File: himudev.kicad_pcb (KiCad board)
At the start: 4 copper layers, 130 parts, among them J1 Conn_01x02, J2 USB_B_Micro, J3 Conn_01x03, J4 20021121-00010C4LF, J5 Conn_02x17_Odd_Even, Q1 IRLML6402, Q2 BSS214NW, Q3 BSS214NW, Q4 BSS214NW, Q5 BSS214NW, Q6 BSS214NW, U1 FT230XS, U2 MCP1726-3302ESN, U3 MIC5319-1.8YD5-TR, U4 IS25WP032D, U5 FE310-G002, U6 ICM-20948, U7 BMP388, X1 KX2132709Z, Y1 TSX-3225 16.0000MF18X-AC0

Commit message: Reload netlist, set part number of J1 and J3
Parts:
- removed C1, C6: 10nF, Capacitor_SMD:C_0805_2012Metric_Pad1.15x1.40mm_HandSolder
- removed C10, C19, C27, C7: 10uF, Capacitor_SMD:C_0805_2012Metric_Pad1.15x1.40mm_HandSolder
- removed C11, C13, C17, C21, C23, C24, C5, C9: 0.1uF, Capacitor_SMD:C_0805_2012Metric_Pad1.15x1.40mm_HandSolder
- removed C12, C15, C20, C22, C25, C26: 1uF, Capacitor_SMD:C_0805_2012Metric_Pad1.15x1.40mm_HandSolder
- removed C14: 2.2uF, Capacitor_SMD:C_0805_2012Metric_Pad1.15x1.40mm_HandSolder
- removed C16, C18: 15pF, Capacitor_SMD:C_0805_2012Metric_Pad1.15x1.40mm_HandSolder
- removed C2, C4: 47pF, Capacitor_SMD:C_0805_2012Metric_Pad1.15x1.40mm_HandSolder
- removed C28, C29, C31, C34: 0.1u, Capacitor_SMD:C_0805_2012Metric_Pad1.15x1.40mm_HandSolder
- removed C3: 4.7uF, Capacitor_SMD:C_0805_2012Metric_Pad1.15x1.40mm_HandSolder
- removed C30, C32, C33: 100n, Capacitor_SMD:C_0805_2012Metric_Pad1.15x1.40mm_HandSolder
- removed C8: 1nF, Capacitor_SMD:C_0805_2012Metric_Pad1.15x1.40mm_HandSolder
- removed D1: NSR05T40XV2T5G, Diode_SMD:D_SOD-523
- removed D10, D9: PESD0603-240, Diode_SMD:D_0603_1608Metric_Pad1.05x0.95mm_HandSolder
- removed D11, D6: Red LTST-C170KRKT, LED_SMD:LED_0805_2012Metric_Pad1.15x1.40mm_HandSolder
- removed D12, D3, D5: Green LTST-C170KGKT, LED_SMD:LED_0805_2012Metric_Pad1.15x1.40mm_HandSolder
- removed D13: Blue LTST-C170TBKT, LED_SMD:LED_0805_2012Metric_Pad1.15x1.40mm_HandSolder
- removed D14, D8: Yellow LTST-C170KSKT, LED_SMD:LED_0805_2012Metric_Pad1.15x1.40mm_HandSolder
- removed D2: SP0502BAHT, Package_TO_SOT_SMD:SOT-23
- removed D4, D7: Orange LTST-C170KFKT, LED_SMD:LED_0805_2012Metric_Pad1.15x1.40mm_HandSolder
- removed FB1: MI0805K601R-10, Resistor_SMD:R_0805_2012Metric_Pad1.15x1.40mm_HandSolder
- removed J1: Conn_01x02, Connector_PinHeader_2.54mm:PinHeader_1x02_P2.54mm_Vertical_SMD_Pin1Left
- removed J2: USB_B_Micro, Connector_USB:USB_Micro-B_Molex-105017-0001
- removed J3: Conn_01x03, Connector_PinHeader_2.54mm:PinHeader_1x03_P2.54mm_Vertical_SMD_Pin1Left
- removed J4: 20021121-00010C4LF, digikey-footprints:PinHeader_2x5_P1.27mm
- removed J5: Conn_02x17_Odd_Even, Connector_PinHeader_2.54mm:PinHeader_2x17_P2.54mm_Vertical_SMD
- removed Q1: IRLML6402, Package_TO_SOT_SMD:SOT-23
- removed Q2, Q3, Q4, Q5, Q6: BSS214NW, Package_TO_SOT_SMD:SOT-323_SC-70
- removed R1, R10, R11, R2, R3, R4, R47, R5, R50, R6, R7, R8, R9: 0, Resistor_SMD:R_0805_2012Metric_Pad1.15x1.40mm_HandSolder
- removed R12, R13: 27, Resistor_SMD:R_0805_2012Metric_Pad1.15x1.40mm_HandSolder
- removed R14, R15, R22: 10k, Resistor_SMD:R_0805_2012Metric_Pad1.15x1.40mm_HandSolder
- removed R16, R20, R27, R29, R30, R31: 100k, Resistor_SMD:R_0805_2012Metric_Pad1.15x1.40mm_HandSolder
- removed R17: 1k, Resistor_SMD:R_0805_2012Metric_Pad1.15x1.40mm_HandSolder
- removed R18, R19, R23, R26, R40, R42, R44, R46: 270, Resistor_SMD:R_0805_2012Metric_Pad1.15x1.40mm_HandSolder
- removed R21, R32, R33, R34, R35, R36, R37, R38, R39, R41, R43, R45: 100, Resistor_SMD:R_0805_2012Metric_Pad1.15x1.40mm_HandSolder
- removed R24, R25: 560, Resistor_SMD:R_0805_2012Metric_Pad1.15x1.40mm_HandSolder
- removed R28: 1M, Resistor_SMD:R_0805_2012Metric_Pad1.15x1.40mm_HandSolder
- removed R48, R49: 4k7, Resistor_SMD:R_0805_2012Metric_Pad1.15x1.40mm_HandSolder
- removed S1, S2: B3F-1000, digikey-footprints:Switch_Tactile_THT_B3F-1xxx
- removed TP1: GND, TestPoint:TestPoint_Pad_D1.5mm
- removed TP2: VBUS, TestPoint:TestPoint_Pad_D1.5mm
- removed TP3: 3V3, TestPoint:TestPoint_Pad_D1.5mm
- removed TP4: FTDI_CBUS0, TestPoint:TestPoint_Pad_D1.5mm
- removed TP5: FTDI_RTS#, TestPoint:TestPoint_Pad_D1.5mm
- removed TP6: FTDI_CTS#, TestPoint:TestPoint_Pad_D1.5mm
- removed TP7: 5V, TestPoint:TestPoint_Pad_D1.5mm
- removed TP8: 1V8, TestPoint:TestPoint_Pad_D1.5mm
- removed TP9: LFALTCLK, TestPoint:TestPoint_Pad_D1.5mm
- removed U1: FT230XS, Package_SO:SSOP-16_3.9x4.9mm_P0.635mm
- removed U2: MCP1726-3302ESN, Package_SO:SOIC-8_3.9x4.9mm_P1.27mm
- removed U3: MIC5319-1.8YD5-TR, Package_TO_SOT_SMD:TSOT-23-5
- removed U4: IS25WP032D, Package_SO:SOIC-8_3.9x4.9mm_P1.27mm
- removed U5: FE310-G002, himudev:QFN-48-1EP_6x6mm_P0.4mm_EP4.2x4.2mm_BigVia
- removed U6: ICM-20948, Sensor_Motion:InvenSense_QFN-24_3x3mm_P0.4mm
- removed U7: BMP388, himudev:Bosch_LGA-10_2x2mm_P0.5mm
- removed X1: KX2132709Z, himudev:KX2132709Z
- removed Y1: TSX-3225 16.0000MF18X-AC0, himudev:TSX-3225

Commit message: Placed component footprints in logical groups
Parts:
- added C1: 10nF, Capacitor_SMD:C_0805_2012Metric_Pad1.15x1.40mm_HandSolder, F.Cu at (76.5, 97.3)
- added C10: 10uF, Capacitor_SMD:C_0805_2012Metric_Pad1.15x1.40mm_HandSolder, F.Cu at (103.9, 69.6)
- added C11: 0.1uF, Capacitor_SMD:C_0805_2012Metric_Pad1.15x1.40mm_HandSolder, F.Cu at (99.7, 105.7)
- added C12: 1uF, Capacitor_SMD:C_0805_2012Metric_Pad1.15x1.40mm_HandSolder, F.Cu at (130.8, -45.0)
- added C13: 0.1uF, Capacitor_SMD:C_0805_2012Metric_Pad1.15x1.40mm_HandSolder, F.Cu at (140.0, -38.9)
- added C14: 2.2uF, Capacitor_SMD:C_0805_2012Metric_Pad1.15x1.40mm_HandSolder, F.Cu at (147.1, -46.7)
- added C15: 1uF, Capacitor_SMD:C_0805_2012Metric_Pad1.15x1.40mm_HandSolder, F.Cu at (163.8, 112.3)
- added C16: 15pF, Capacitor_SMD:C_0805_2012Metric_Pad1.15x1.40mm_HandSolder, F.Cu at (153.2, 131.6)
- added C17: 0.1uF, Capacitor_SMD:C_0805_2012Metric_Pad1.15x1.40mm_HandSolder, F.Cu at (190.2, 146.8)
- added C18: 15pF, Capacitor_SMD:C_0805_2012Metric_Pad1.15x1.40mm_HandSolder, F.Cu at (157.9, 131.6)
- added C19: 10uF, Capacitor_SMD:C_0805_2012Metric_Pad1.15x1.40mm_HandSolder, F.Cu at (164.6, 44.2)
- added C2: 47pF, Capacitor_SMD:C_0805_2012Metric_Pad1.15x1.40mm_HandSolder, F.Cu at (80.5, 107.7)
- added C20: 1uF, Capacitor_SMD:C_0805_2012Metric_Pad1.15x1.40mm_HandSolder, F.Cu at (164.6, 47.8)
- added C21: 0.1uF, Capacitor_SMD:C_0805_2012Metric_Pad1.15x1.40mm_HandSolder, F.Cu at (164.6, 51.4)
- added C22: 1uF, Capacitor_SMD:C_0805_2012Metric_Pad1.15x1.40mm_HandSolder, F.Cu at (169.7, 51.6)
- added C23: 0.1uF, Capacitor_SMD:C_0805_2012Metric_Pad1.15x1.40mm_HandSolder, F.Cu at (175.5, 51.6)
- added C24: 0.1uF, Capacitor_SMD:C_0805_2012Metric_Pad1.15x1.40mm_HandSolder, F.Cu at (180.1, 51.6)
- added C25: 1uF, Capacitor_SMD:C_0805_2012Metric_Pad1.15x1.40mm_HandSolder, F.Cu at (175.5, 47.5)
- added C26: 1uF, Capacitor_SMD:C_0805_2012Metric_Pad1.15x1.40mm_HandSolder, F.Cu at (180.1, 48.0)
- added C27: 10uF, Capacitor_SMD:C_0805_2012Metric_Pad1.15x1.40mm_HandSolder, F.Cu at (175.8, 43.9)
- added C28: 0.1u, Capacitor_SMD:C_0805_2012Metric_Pad1.15x1.40mm_HandSolder, F.Cu at (200.2, -73.8)
- added C29: 0.1u, Capacitor_SMD:C_0805_2012Metric_Pad1.15x1.40mm_HandSolder, F.Cu at (195.4, -68.6)
- added C3: 4.7uF, Capacitor_SMD:C_0805_2012Metric_Pad1.15x1.40mm_HandSolder, F.Cu at (99.6, 111.2)
- added C30: 100n, Capacitor_SMD:C_0805_2012Metric_Pad1.15x1.40mm_HandSolder, F.Cu at (200.6, -76.7)
- added C31: 0.1u, Capacitor_SMD:C_0805_2012Metric_Pad1.15x1.40mm_HandSolder, F.Cu at (195.4, -71.6)
- added C32: 100n, Capacitor_SMD:C_0805_2012Metric_Pad1.15x1.40mm_HandSolder, F.Cu at (222.8, -60.2)
- added C33: 100n, Capacitor_SMD:C_0805_2012Metric_Pad1.15x1.40mm_HandSolder, F.Cu at (229.9, -67.8)
- added C34: 0.1u, Capacitor_SMD:C_0805_2012Metric_Pad1.15x1.40mm_HandSolder, F.Cu at (230.1, -64.3)
- added C4: 47pF, Capacitor_SMD:C_0805_2012Metric_Pad1.15x1.40mm_HandSolder, F.Cu at (80.5, 100.8)
- added C5: 0.1uF, Capacitor_SMD:C_0805_2012Metric_Pad1.15x1.40mm_HandSolder, F.Cu at (94.9, 114.0)
- added C6: 10nF, Capacitor_SMD:C_0805_2012Metric_Pad1.15x1.40mm_HandSolder, F.Cu at (108.5, 107.5)
- added C7: 10uF, Capacitor_SMD:C_0805_2012Metric_Pad1.15x1.40mm_HandSolder, F.Cu at (100.3, 62.5)
- added C8: 1nF, Capacitor_SMD:C_0805_2012Metric_Pad1.15x1.40mm_HandSolder, F.Cu at (103.1, 65.8)
- added C9: 0.1uF, Capacitor_SMD:C_0805_2012Metric_Pad1.15x1.40mm_HandSolder, F.Cu at (95.6, 96.5)
- added D1: NSR05T40XV2T5G, Diode_SMD:D_SOD-523, F.Cu at (75.7, 129.8)
- added D10: PESD0603-240, Diode_SMD:D_0603_1608Metric_Pad1.05x0.95mm_HandSolder, F.Cu at (222.5, 163.8)
- added D11: Red LTST-C170KRKT, LED_SMD:LED_0805_2012Metric_Pad1.15x1.40mm_HandSolder, F.Cu at (174.0, 75.9)
- added D12: Green LTST-C170KGKT, LED_SMD:LED_0805_2012Metric_Pad1.15x1.40mm_HandSolder, F.Cu at (178.1, 75.7)
- added D13: Blue LTST-C170TBKT, LED_SMD:LED_0805_2012Metric_Pad1.15x1.40mm_HandSolder, F.Cu at (182.4, 75.7)
- added D14: Yellow LTST-C170KSKT, LED_SMD:LED_0805_2012Metric_Pad1.15x1.40mm_HandSolder, F.Cu at (186.7, 76.2)
- added D2: SP0502BAHT, Package_TO_SOT_SMD:SOT-23, F.Cu at (79.5, 129.0)
- added D3: Green LTST-C170KGKT, LED_SMD:LED_0805_2012Metric_Pad1.15x1.40mm_HandSolder, F.Cu at (109.7, 98.5)
- added D4: Orange LTST-C170KFKT, LED_SMD:LED_0805_2012Metric_Pad1.15x1.40mm_HandSolder, F.Cu at (104.3, 103.0)
- added D5: Green LTST-C170KGKT, LED_SMD:LED_0805_2012Metric_Pad1.15x1.40mm_HandSolder, F.Cu at (91.2, -13.0)
- added D6: Red LTST-C170KRKT, LED_SMD:LED_0805_2012Metric_Pad1.15x1.40mm_HandSolder, F.Cu at (90.9, -8.89)
- added D7: Orange LTST-C170KFKT, LED_SMD:LED_0805_2012Metric_Pad1.15x1.40mm_HandSolder, F.Cu at (91.2, -5.08)
- added D8: Yellow LTST-C170KSKT, LED_SMD:LED_0805_2012Metric_Pad1.15x1.40mm_HandSolder, F.Cu at (90.9, -1.02)
- added D9: PESD0603-240, Diode_SMD:D_0603_1608Metric_Pad1.05x0.95mm_HandSolder, F.Cu at (172.7, 163.6)
- added FB1: MI0805K601R-10, Resistor_SMD:R_0805_2012Metric_Pad1.15x1.40mm_HandSolder, F.Cu at (88.9, 88.6)
- added J1: M20-8770642R, Connector_PinHeader_2.54mm:PinHeader_1x02_P2.54mm_Vertical_SMD_Pin1Left, F.Cu at (72.9, 124.0)
- added J2: USB_B_Micro, Connector_USB:USB_Micro-B_Molex-105017-0001, F.Cu at (72.6, 105.0)
- added J3: M20-8770642R, Connector_PinHeader_2.54mm:PinHeader_1x03_P2.54mm_Vertical_SMD_Pin1Left, F.Cu at (80.0, 89.4)
- added J4: 20021121-00010C4LF, digikey-footprints:PinHeader_2x5_P1.27mm, F.Cu at (151.6, 162.1)
- added J5: M20-8762042, Connector_PinHeader_2.54mm:PinHeader_2x17_P2.54mm_Vertical_SMD, F.Cu at (210.1, 104.6)
- added Q1: IRLML6402, Package_TO_SOT_SMD:SOT-23, F.Cu at (104.9, 112.6)
- added Q2: BSS214NW, Package_TO_SOT_SMD:SOT-323_SC-70, F.Cu at (86.6, -13.0)
- added Q3: BSS214NW, Package_TO_SOT_SMD:SOT-323_SC-70, F.Cu at (174.0, 80.3)
- added Q4: BSS214NW, Package_TO_SOT_SMD:SOT-323_SC-70, F.Cu at (178.1, 80.0)
- added Q5: BSS214NW, Package_TO_SOT_SMD:SOT-323_SC-70, F.Cu at (182.4, 80.5)
- added Q6: BSS214NW, Package_TO_SOT_SMD:SOT-323_SC-70, F.Cu at (186.7, 80.5)
- added R1: 0, Resistor_SMD:R_0805_2012Metric_Pad1.15x1.40mm_HandSolder, F.Cu at (165.2, -24.0)
- added R10: 0, Resistor_SMD:R_0805_2012Metric_Pad1.15x1.40mm_HandSolder, F.Cu at (160.5, -21.0)
- added R11: 0, Resistor_SMD:R_0805_2012Metric_Pad1.15x1.40mm_HandSolder, F.Cu at (160.5, -24.0)
- added R12: 27, Resistor_SMD:R_0805_2012Metric_Pad1.15x1.40mm_HandSolder, F.Cu at (80.5, 105.4)
- added R13: 27, Resistor_SMD:R_0805_2012Metric_Pad1.15x1.40mm_HandSolder, F.Cu at (80.5, 103.1)
- added R14: 10k, Resistor_SMD:R_0805_2012Metric_Pad1.15x1.40mm_HandSolder, F.Cu at (104.6, 107.4)
- added R15: 10k, Resistor_SMD:R_0805_2012Metric_Pad1.15x1.40mm_HandSolder, F.Cu at (96.0, 63.0)
- added R16: 100k, Resistor_SMD:R_0805_2012Metric_Pad1.15x1.40mm_HandSolder, F.Cu at (100.1, 100.9)
- added R17: 1k, Resistor_SMD:R_0805_2012Metric_Pad1.15x1.40mm_HandSolder, F.Cu at (100.3, 96.8)
- added R18: 270, Resistor_SMD:R_0805_2012Metric_Pad1.15x1.40mm_HandSolder, F.Cu at (90.1, 117.1)
- added R19: 270, Resistor_SMD:R_0805_2012Metric_Pad1.15x1.40mm_HandSolder, F.Cu at (94.9, 111.1)
- added R2: 0, Resistor_SMD:R_0805_2012Metric_Pad1.15x1.40mm_HandSolder, F.Cu at (160.5, -18.1)
- added R20: 100k, Resistor_SMD:R_0805_2012Metric_Pad1.15x1.40mm_HandSolder, F.Cu at (95.5, 116.9)
- added R21: 100, Resistor_SMD:R_0805_2012Metric_Pad1.15x1.40mm_HandSolder, F.Cu at (82.5, -13.0)
- added R22: 10k, Resistor_SMD:R_0805_2012Metric_Pad1.15x1.40mm_HandSolder, F.Cu at (145.8, -41.9)
- added R23: 270, Resistor_SMD:R_0805_2012Metric_Pad1.15x1.40mm_HandSolder, F.Cu at (96.0, -13.0)
- added R24: 560, Resistor_SMD:R_0805_2012Metric_Pad1.15x1.40mm_HandSolder, F.Cu at (96.0, -8.89)
- added R25: 560, Resistor_SMD:R_0805_2012Metric_Pad1.15x1.40mm_HandSolder, F.Cu at (96.0, -5.08)
- added R26: 270, Resistor_SMD:R_0805_2012Metric_Pad1.15x1.40mm_HandSolder, F.Cu at (96.0, -1.02)
- added R27: 100k, Resistor_SMD:R_0805_2012Metric_Pad1.15x1.40mm_HandSolder, F.Cu at (173.5, 160.3)
- added R28: 1M, Resistor_SMD:R_0805_2012Metric_Pad1.15x1.40mm_HandSolder, F.Cu at (155.2, 135.4)
- added R29: 100k, Resistor_SMD:R_0805_2012Metric_Pad1.15x1.40mm_HandSolder, F.Cu at (162.1, 102.1)
- added R3: 0, Resistor_SMD:R_0805_2012Metric_Pad1.15x1.40mm_HandSolder, F.Cu at (165.2, -21.0)
- added R30: 100k, Resistor_SMD:R_0805_2012Metric_Pad1.15x1.40mm_HandSolder, F.Cu at (166.4, 102.9)
- added R31: 100k, Resistor_SMD:R_0805_2012Metric_Pad1.15x1.40mm_HandSolder, F.Cu at (223.5, 159.8)
- added R32: 100, Resistor_SMD:R_0805_2012Metric_Pad1.15x1.40mm_HandSolder, F.Cu at (144.5, 159.2)
- added R33: 100, Resistor_SMD:R_0805_2012Metric_Pad1.15x1.40mm_HandSolder, F.Cu at (149.3, 156.2)
- added R34: 100, Resistor_SMD:R_0805_2012Metric_Pad1.15x1.40mm_HandSolder, F.Cu at (144.5, 156.2)
- added R35: 100, Resistor_SMD:R_0805_2012Metric_Pad1.15x1.40mm_HandSolder, F.Cu at (149.3, 153.3)
- added R36: 100, Resistor_SMD:R_0805_2012Metric_Pad1.15x1.40mm_HandSolder, F.Cu at (180.3, 43.9)
- added R37: 100, Resistor_SMD:R_0805_2012Metric_Pad1.15x1.40mm_HandSolder, F.Cu at (198.1, 107.2)
- added R38: 100, Resistor_SMD:R_0805_2012Metric_Pad1.15x1.40mm_HandSolder, F.Cu at (198.2, 111.0)
- added R39: 100, Resistor_SMD:R_0805_2012Metric_Pad1.15x1.40mm_HandSolder, F.Cu at (173.2, 85.3)
- added R4: 0, Resistor_SMD:R_0805_2012Metric_Pad1.15x1.40mm_HandSolder, F.Cu at (170.0, -24.0)
- added R40: 270, Resistor_SMD:R_0805_2012Metric_Pad1.15x1.40mm_HandSolder, F.Cu at (174.0, 71.9)
- added R41: 100, Resistor_SMD:R_0805_2012Metric_Pad1.15x1.40mm_HandSolder, F.Cu at (177.3, 85.3)
- added R42: 270, Resistor_SMD:R_0805_2012Metric_Pad1.15x1.40mm_HandSolder, F.Cu at (178.1, 71.6)
- added R43: 100, Resistor_SMD:R_0805_2012Metric_Pad1.15x1.40mm_HandSolder, F.Cu at (181.6, 85.6)
- added R44: 270, Resistor_SMD:R_0805_2012Metric_Pad1.15x1.40mm_HandSolder, F.Cu at (182.4, 71.4)
- added R45: 100, Resistor_SMD:R_0805_2012Metric_Pad1.15x1.40mm_HandSolder, F.Cu at (185.9, 85.6)
- added R46: 270, Resistor_SMD:R_0805_2012Metric_Pad1.15x1.40mm_HandSolder, F.Cu at (186.7, 71.4)
- added R47: 0, Resistor_SMD:R_0805_2012Metric_Pad1.15x1.40mm_HandSolder, F.Cu at (191.0, -81.0)
- added R48: 4k7, Resistor_SMD:R_0805_2012Metric_Pad1.15x1.40mm_HandSolder, F.Cu at (216.7, -66.3)
- added R49: 4k7, Resistor_SMD:R_0805_2012Metric_Pad1.15x1.40mm_HandSolder, F.Cu at (216.9, -62.5)
- added R5: 0, Resistor_SMD:R_0805_2012Metric_Pad1.15x1.40mm_HandSolder, F.Cu at (165.2, -18.1)
- added R50: 0, Resistor_SMD:R_0805_2012Metric_Pad1.15x1.40mm_HandSolder, F.Cu at (222.8, -69.3)
- added R6: 0, Resistor_SMD:R_0805_2012Metric_Pad1.15x1.40mm_HandSolder, F.Cu at (170.0, -21.0)
- added R7: 0, Resistor_SMD:R_0805_2012Metric_Pad1.15x1.40mm_HandSolder, F.Cu at (174.7, -24.0)
- added R8: 0, Resistor_SMD:R_0805_2012Metric_Pad1.15x1.40mm_HandSolder, F.Cu at (170.0, -18.1)
- added R9: 0, Resistor_SMD:R_0805_2012Metric_Pad1.15x1.40mm_HandSolder, F.Cu at (174.7, -21.0)
- added S1: PTS645SM43SMTR92_LFS, digikey-footprints:Switch_Tactile_SMD_6x6mm_PTS645, F.Cu at (180.0, 162.0)
- added S2: PTS645SM43SMTR92_LFS, digikey-footprints:Switch_Tactile_SMD_6x6mm_PTS645, F.Cu at (215.6, 162.0)
- added TP1: GND, TestPoint:TestPoint_Pad_D1.5mm, F.Cu at (71.9, 98.3)
- added TP2: VBUS, TestPoint:TestPoint_Pad_D1.5mm, F.Cu at (81.8, 82.5)
- added TP3: 3V3, TestPoint:TestPoint_Pad_D1.5mm, F.Cu at (105.2, 62.7)
- added TP4: FTDI_CBUS0, TestPoint:TestPoint_Pad_D1.5mm, F.Cu at (123.4, 105.6)
- added TP5: FTDI_RTS#, TestPoint:TestPoint_Pad_D1.5mm, F.Cu at (117.8, 111.0)
- added TP6: FTDI_CTS#, TestPoint:TestPoint_Pad_D1.5mm, F.Cu at (100.4, 116.4)
- added TP7: 5V, TestPoint:TestPoint_Pad_D1.5mm, F.Cu at (117.1, 115.1)
- added TP8: 1V8, TestPoint:TestPoint_Pad_D1.5mm, F.Cu at (151.9, -42.9)
- added TP9: LFALTCLK, TestPoint:TestPoint_Pad_D1.5mm, F.Cu at (194.1, 142.5)
- added U1: FT230XS, Package_SO:SSOP-16_3.9x4.9mm_P0.635mm, F.Cu at (93.7, 104.9)
- added U2: MCP1726-3302ESN, Package_SO:SOIC-8_3.9x4.9mm_P1.27mm, F.Cu at (96.9, 69.2)
- added U3: MIC5319-1.8YD5-TR, Package_TO_SOT_SMD:TSOT-23-5, F.Cu at (139.4, -45.5)
- added U4: IS25WP032D, Package_SO:SOIC-8_3.9x4.9mm_P1.27mm, F.Cu at (164.3, 107.4)
- added U5: FE310-G002, himudev:QFN-48-1EP_6x6mm_P0.4mm_EP4.2x4.2mm_BigVia, F.Cu at (182.4, 119.4)
- added U6: ICM-20948, Sensor_Motion:InvenSense_QFN-24_3x3mm_P0.4mm, F.Cu at (190.9, -75.6)
- added U7: BMP388, himudev:Bosch_LGA-10_2x2mm_P0.5mm, F.Cu at (223.0, -64.8)
- added X1: KX2132709Z, himudev:KX2132709Z, F.Cu at (190.2, 143.5)
- added Y1: TSX-3225 16.0000MF18X-AC0, himudev:TSX-3225, F.Cu at (164.6, 129.3)
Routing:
- net Net-(TP9-Pad1): track 0.00 -> 2.57 mm
- net GND: track 0.00 -> 2.40 mm
- net +3V3: track 0.00 -> 2.40 mm
- net Net-(C32-Pad2): track 0.00 -> 1.73 mm
- net (no net): vias 0 -> 3

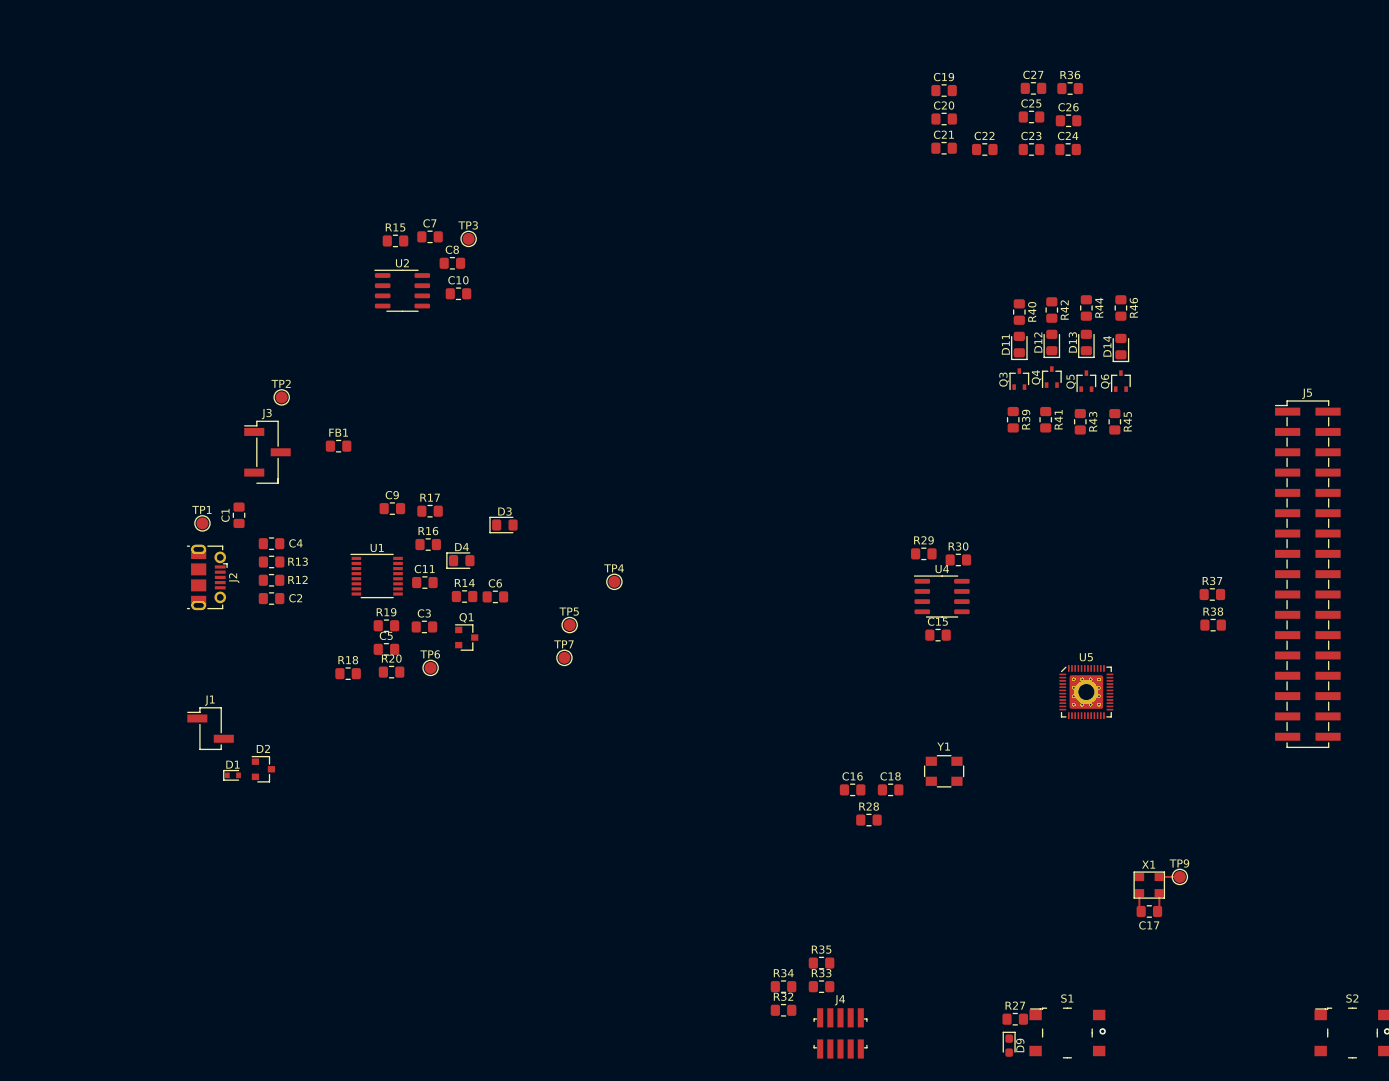
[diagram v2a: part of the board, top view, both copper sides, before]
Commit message: Changed main header from 34 to 32 pin, added board outline
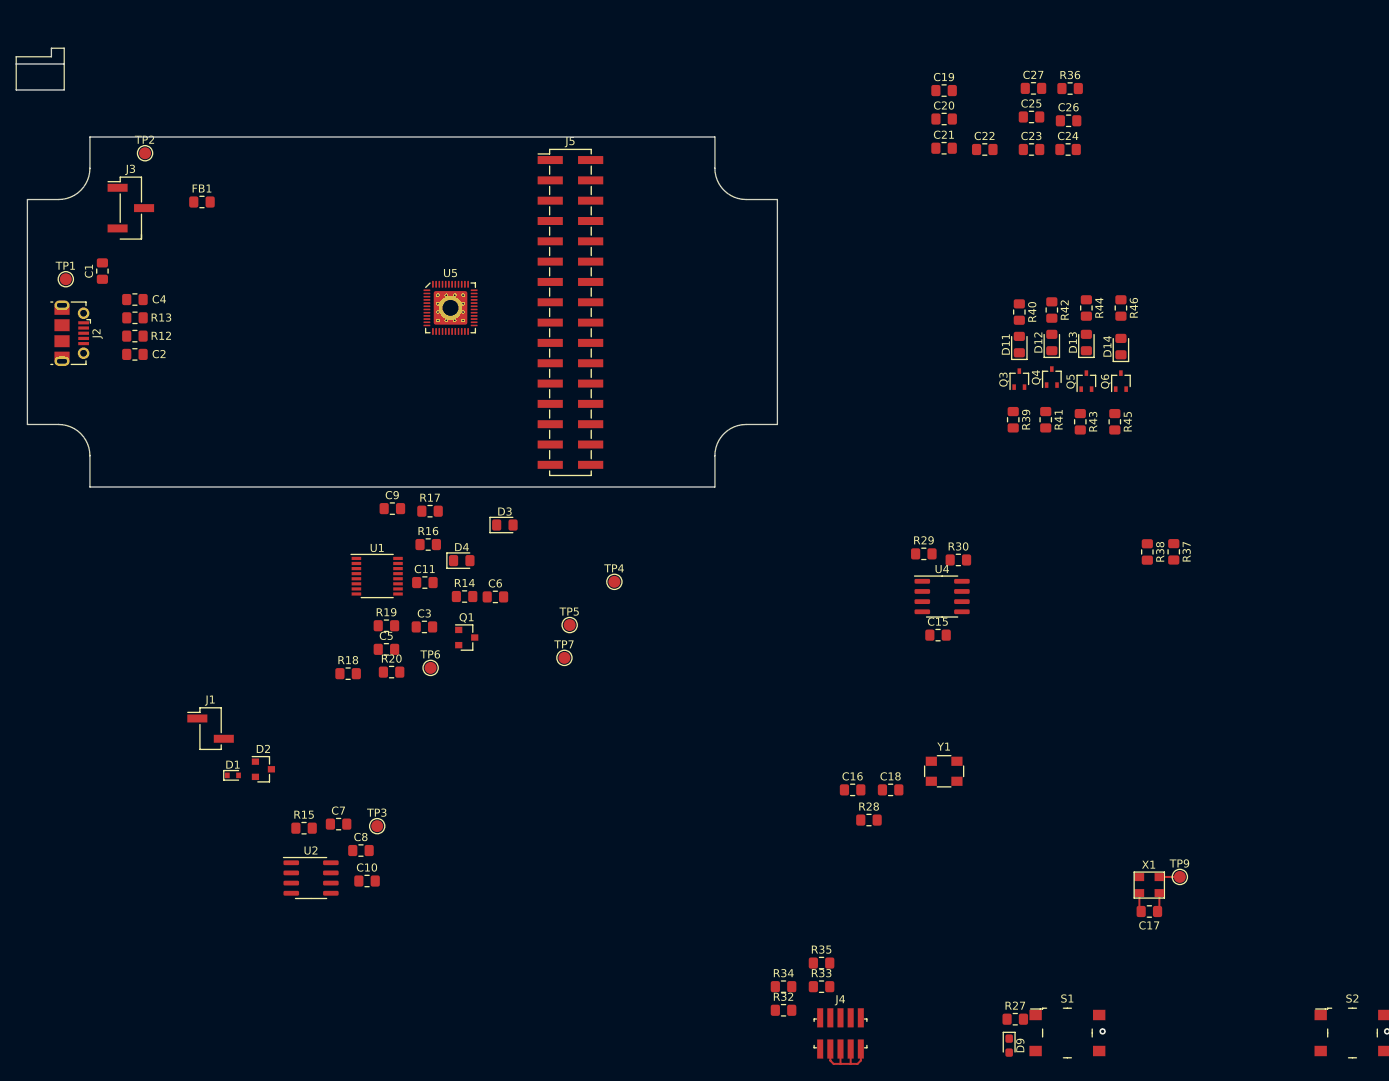
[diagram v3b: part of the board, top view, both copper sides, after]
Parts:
- J5: footprint Connector_PinHeader_2.54mm:PinHeader_2x17_P2.54mm_Vertical_SMD -> Connector_PinHeader_2.54mm:PinHeader_2x16_P2.54mm_Vertical_SMD
- moved J5 97.8 mm to (117.9, 71.9)
- moved U5 92.9 mm to (102.9, 71.4)
- moved R15 74.3 mm to (84.6, 136.4)
- moved TP3 74.3 mm to (93.7, 136.1)
- moved C10 74.3 mm to (92.5, 143.0)
- moved C8 74.3 mm to (91.7, 139.2)
- moved U2 74.3 mm to (85.5, 142.6)
- moved C7 74.3 mm to (88.9, 135.9)
- moved FB1 35.0 mm to (71.8, 58.1)
- moved J2 35.0 mm to (55.6, 74.5)
- moved J3 35.0 mm to (62.9, 58.9)
- moved C2 35.0 mm to (63.4, 77.2)
- moved C4 35.0 mm to (63.4, 70.3)
- moved R12 35.0 mm to (63.4, 74.9)
- moved R13 35.0 mm to (63.4, 72.6)
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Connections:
- J5 pad 13: Net-(J5-Pad13) -> GND
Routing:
- net GND: track 2.40 -> 13.2 mm
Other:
- board outline added: 95.2 x 54.9 mm

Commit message: Placed pressure sensor, connector changed to USB-C
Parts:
- added R51: 5k1, Resistor_SMD:R_0805_2012Metric_Pad1.15x1.40mm_HandSolder, F.Cu at (116.6, 107.3)
- added R52: 5k1, Resistor_SMD:R_0805_2012Metric_Pad1.15x1.40mm_HandSolder, F.Cu at (116.6, 95.9)
- J2: value USB_B_Micro -> USB_C16PIN; footprint Connector_USB:USB_Micro-B_Molex-105017-0001 -> USB-C-16pin:USB-C-COM-15111
- moved C20 236.5 mm to (167.8, -188.7)
- moved R29 236.5 mm to (165.2, -134.4)
- moved R30 236.5 mm to (169.5, -133.6)
- moved R36 236.5 mm to (183.5, -192.5)
- moved R38 236.5 mm to (193.2, -134.6)
- moved R40 236.5 mm to (177.2, -164.6)
- moved C15 236.5 mm to (167.0, -124.2)
- moved C19 236.5 mm to (167.8, -192.3)
- moved C21 236.5 mm to (167.8, -185.1)
- moved C22 236.5 mm to (172.8, -184.9)
- moved C23 236.5 mm to (178.7, -184.9)
- moved C24 236.5 mm to (183.3, -184.9)
- moved C25 236.5 mm to (178.7, -189.0)
- moved C26 236.5 mm to (183.3, -188.5)
- moved C27 236.5 mm to (178.9, -192.6)
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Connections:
- C2 pad 1: Net-(C2-Pad1) -> /USB_Power/USB_D+
- C4 pad 1: Net-(C4-Pad1) -> /USB_Power/USB_D-
- R12 pad 2: Net-(C2-Pad1) -> /USB_Power/USB_D+
- R13 pad 2: Net-(C4-Pad1) -> /USB_Power/USB_D-
- R48 pad 1: +3V3 -> Net-(C32-Pad2)
- R49 pad 1: +3V3 -> Net-(C32-Pad2)
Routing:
- net GND: track 13.2 -> 41.6 mm, vias 0 -> 11
- net Net-(C32-Pad2): track 1.73 -> 28.8 mm
- net Net-(C1-Pad1): track 0.00 -> 24.8 mm, vias 0 -> 2
- net /Sensors/BMP_INT: track 0.00 -> 15.2 mm
- net /Sensors/BMP_SCL: track 0.00 -> 12.5 mm, vias 0 -> 2
- net /MCU_clk_reset/I2C_SDA: track 0.00 -> 10.9 mm
- net /Sensors/BMP_SDA: track 0.00 -> 10.5 mm
- net /USB_Power/USB_D-: track 0.00 -> 10.2 mm
- net /USB_Power/USB_D+: track 0.00 -> 8.40 mm
- net Net-(J2-PadA5): track 0.00 -> 7.49 mm
- net VIN: track 0.00 -> 7.36 mm
- net +3V3: track 2.40 -> 9.33 mm
- net Net-(J2-PadB5): track 0.00 -> 6.82 mm
- net /MCU_clk_reset/I2C_INT: track 0.00 -> 6.11 mm
- net /MCU_clk_reset/I2C_SCL: track 0.00 -> 5.26 mm
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- added copper zone on In2.Cu, net +3V3
- added copper zone on In1.Cu, net GND
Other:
- board size 95.2 x 54.9 mm -> 93.6 x 43.6 mm
- net class Default: clearance 0.2 -> 0.254; trace_width 0.25 -> 0.254; via_dia 0.8 -> 0.508; via_drill 0.4 -> 0.254
- rule pad_to_mask_clearance: 0.051 -> 0.0889
- rule solder_mask_min_width: 0.25 -> 0.0889
- rule trace_clearance: 0.2 -> 0.254
- rule trace_min: 0.2 -> 0.127
- rule via_min_drill: 0.3 -> 0.254
- rule via_min_size: 0.4 -> 0.508

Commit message: Route power traces on the inner layer
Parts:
- moved TP3 213.6 mm to (145.8, 86.0)
- moved U2 208.6 mm to (129.5, 87.1), turned to 270 degrees
- moved C10 205.5 mm to (133.7, 88.9), turned to 90 degrees
- moved R15 203.0 mm to (125.6, 87.6), turned to 90 degrees
- moved C7 200.7 mm to (125.6, 83.4), turned to 270 degrees
- moved C8 198.3 mm to (128.3, 91.9), turned to 180 degrees
- moved Q1 171.1 mm to (122.9, 91.6), turned to 270 degrees
- moved R17 29.9 mm to (-27.7, 159.5)
- moved R16 22.8 mm to (-29.6, 156.3)
- moved C11 16.5 mm to (-34.2, 156.2)
- moved R20 15.3 mm to (-33.3, 159.5)
- moved TP1 8.38 mm to (108.7, 108.6)
- moved TP2 7.77 mm to (122.3, 82.5)
- moved U5 5.92 mm to (165.1, 101.6)
- moved R7 3.59 mm to (177.3, -21.4)
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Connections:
- C11 pad 1: VIN -> +5V
- C7 pad 1: VIN -> +5V
- D1 pad 2: VIN -> VINP
- J1 pad 1: VIN -> VINP
- J5 pad 1: VIN -> VINP
- J5 pad 3: VIN -> +5V
- Q1 pad 3: VIN -> +5V
- R15 pad 1: VIN -> +5V
- R20 pad 1: VIN -> +5V
- R25 pad 1: VIN -> +5V
- TP7 pad 1: VIN -> +5V
- U2 pad 1: VIN -> +5V
- U2 pad 2: VIN -> +5V
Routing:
- net VBUS: track 0.00 -> 85.5 mm, vias 0 -> 3
- net VINP: track 0.00 -> 84.5 mm, vias 0 -> 2
- net +5V: track 0.00 -> 60.4 mm, vias 0 -> 1
- net VIN: track 7.36 -> 0.00 mm
- net Net-(C1-Pad1): track 24.8 -> 29.0 mm, vias 2 -> 4
- net +3V3: track 9.33 -> 12.4 mm, vias 0 -> 1
- net Net-(C3-Pad1): track 0.00 -> 2.22 mm
- net GND: track 41.6 -> 42.3 mm
- net /USB_Power/USB_D+: track 8.40 -> 8.91 mm
- net Net-(J2-PadB5): track 6.82 -> 7.33 mm
- net /USB_Power/USB_D-: track 10.2 -> 10.7 mm
- net Net-(J2-PadA5): track 7.49 -> 7.99 mm
- added copper zone on F.Cu, net GND
